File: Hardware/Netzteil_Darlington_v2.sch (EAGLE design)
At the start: 149 parts, among them IC1 7815TV, IC11 OPA2197, IC12 MAX4080F, IC13 OPA2197, IC15 LD33V, IC17 7815TV, IC18 7812TV, IC2 OPA2197, IC4 LM358ADR, IC5 OPA2197, IC6 TPS5430, IC9 LM334, T1 IRLL110TRPBF, T3 BD139, T4 2N5401, T5 TIP3055, T6 TIP3055, T7 BD139, T8 BC847ALT1G, T9 BUJ303B,127

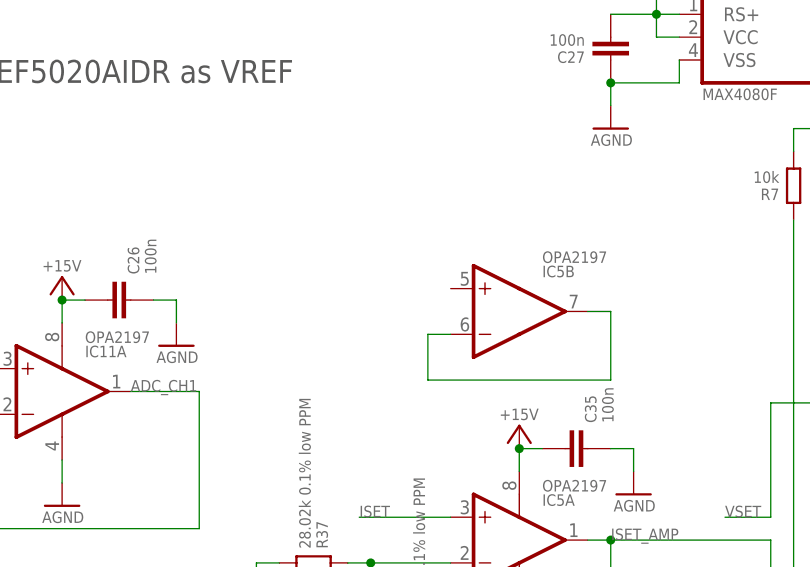
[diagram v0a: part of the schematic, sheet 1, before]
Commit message: Add files via upload
fix second, floating, unused ISET opamp (IC5B)
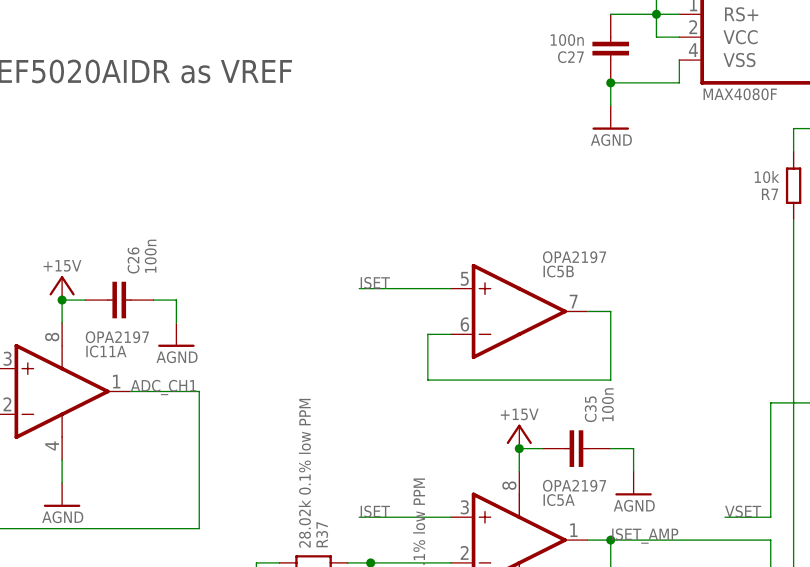
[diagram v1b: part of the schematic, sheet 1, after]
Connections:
- net ISET: now also IC5B.+IN
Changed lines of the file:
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@@
 <setting verticaltext="up"/>
 </settings>
-<grid distance="1.27" unitdist="mm" unit="mm" style="lines" multiple="1" display="yes" altdistance="0.01" altunitdist="inch" altunit="inch"/>
+<grid distance="2.54" unitdist="mm" unit="mm" style="lines" multiple="1" display="yes" altdistance="0.01" altunitdist="inch" altunit="inch"/>
 <layers>
 <layer number="1" name="Top" color="4" fill="1" visible="no" active="no"/>
@@
 <label x="86.36" y="96.52" size="1.27" layer="95"/>
 </segment>
-</net>
+<segment>
+<pinref part="IC5" gate="B" pin="+IN"/>
+<wire x1="96.52" y1="121.92" x2="86.36" y2="121.92" width="0.1524" layer="91"/>
+<label x="86.36" y="121.92" size="1.27" layer="95"/>
+</segment>
+</net>

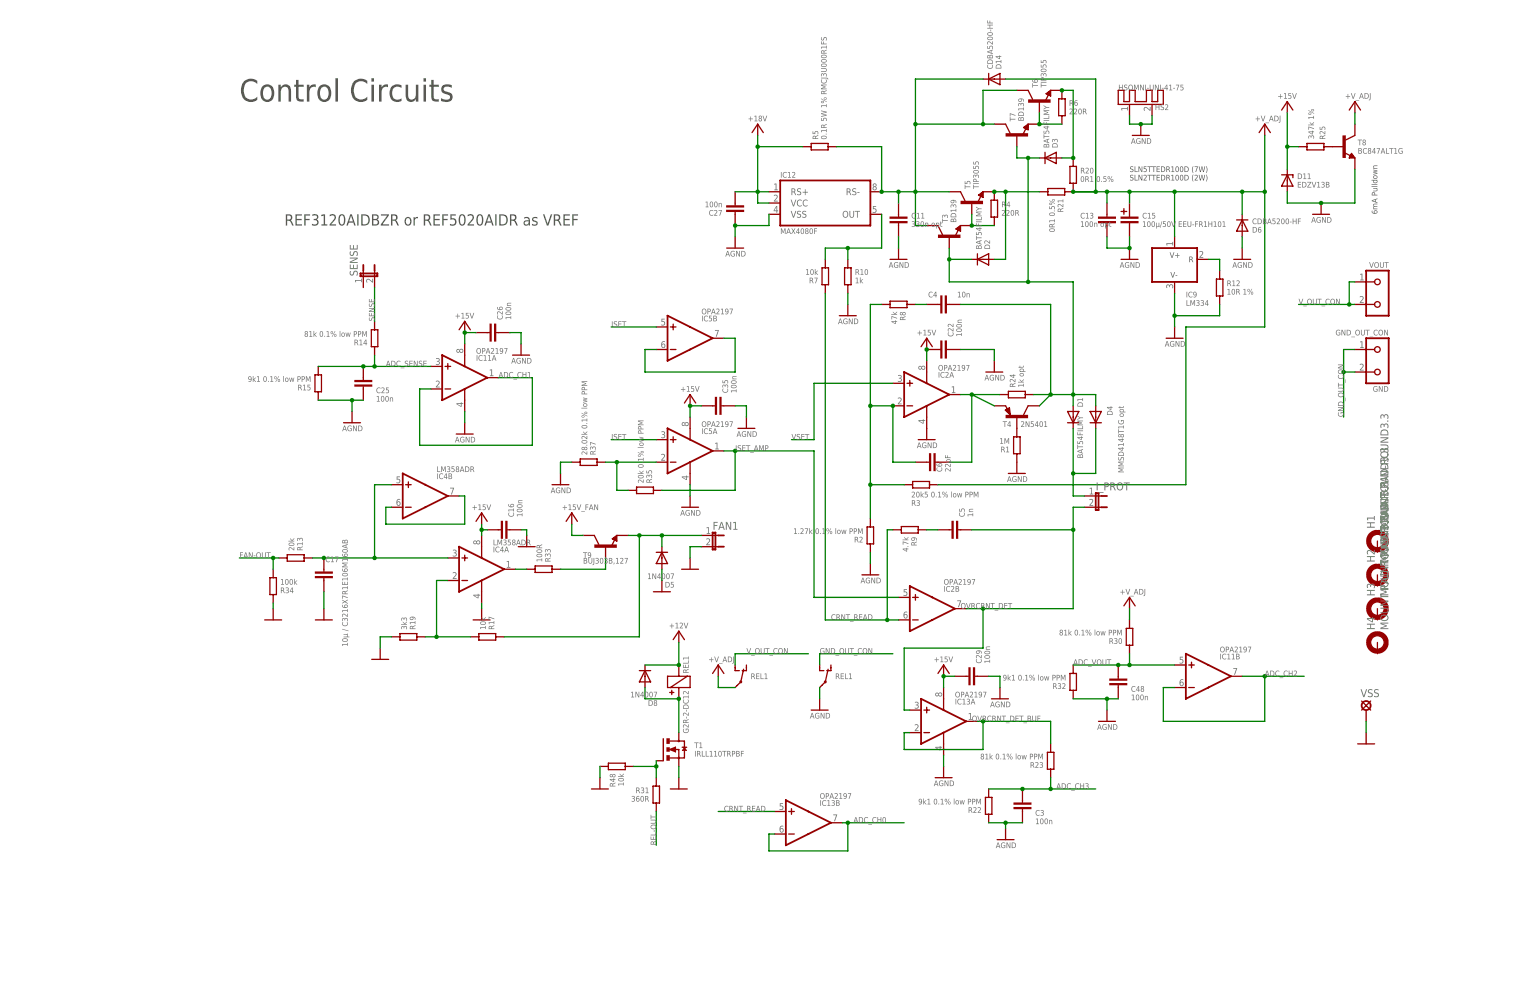
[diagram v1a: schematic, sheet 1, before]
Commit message: update to rev 1.6
fix several bugs and issues
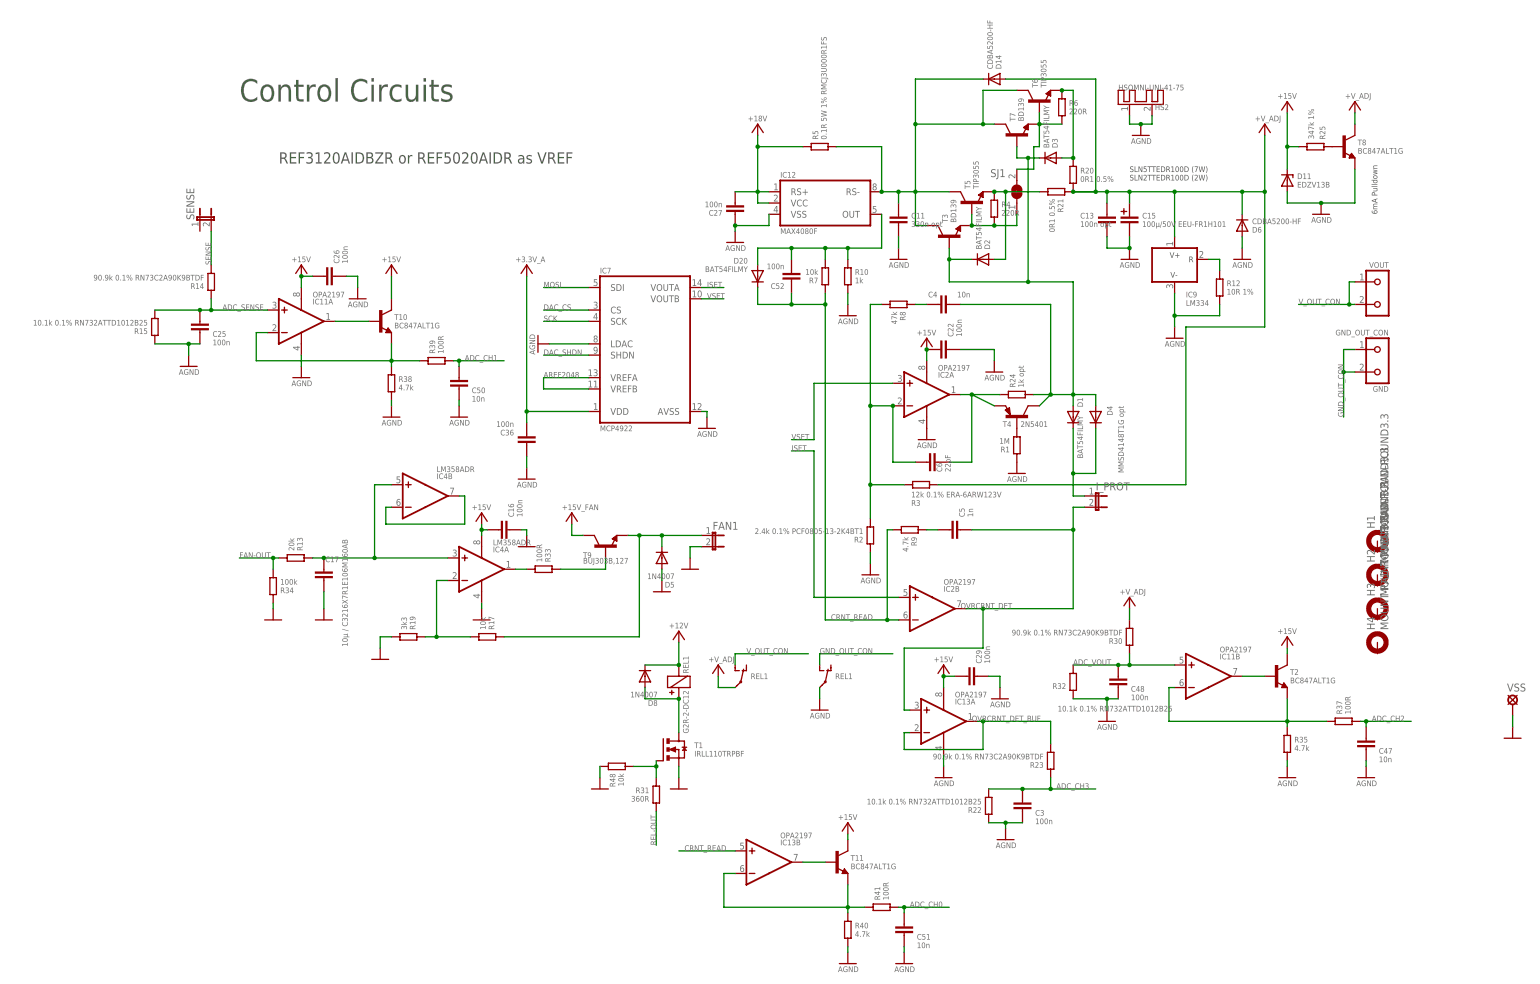
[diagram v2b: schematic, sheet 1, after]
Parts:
- removed ETHERNET: (no value), con-lsta:FE08-1
- added C36, C46, C52: 100n, goujine:CC/0805
- added C44, C45: 10µ / C3216X7R1E106M160AB, goujine:CC/1206
- added C47, C50, C51: 10n, goujine:CC/0805
- added D13: 1N4007, diode:DIODE-DO214AA
- added D20: BAT54FILMY, neumluc:DBAT54FILMY
- added ESP: (no value), con-lstb:MA06-1
- added IC7: MCP4922, neumluc:MCP4922
- added L5: MPZ2012S601AT000, neumluc:L0805
- added R38, R40: 4.7k, neumluc:R-SMD0805
- added R39, R41: 100R, neumluc:R-SMD0805
- added SJ1: (no value), jumper:SJ
- added T10, T11, T2: BC847ALT1G, neumluc:T-NPNSOT23-BEC
- IC5: value OPA2197 -> LD33V; device goujine:DUAL-OPVSOP8 -> neumluc:LD33V
- R14, R23, R30: value 81k 0.1% low PPM -> 90.9k 0.1% RN73C2A90K9BTDF
- R15, R22, R32: value 9k1 0.1% low PPM -> 10.1k 0.1% RN732ATTD1012B25
- R18: value 2k5 -> 2k2
- R2: value 1.27k 0.1% low PPM -> 2.4k 0.1% PCF0805-13-2K4BT1
- R3: value 20k5 0.1% low PPM -> 12k 0.1% ERA-6ARW123V
- R35: value 20k 0.1% low PPM -> 4.7k
- R37: value 28.02k 0.1% low PPM -> 100R
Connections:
- removed net +3.3V_LP: C7.1, C8.1, IC3.IN, U$33.3V3_LO
- removed net ETH_CS: ETHERNET.6, U$33.28
- removed net ETH_INT: ETHERNET.4, U$33.25
- removed net ETH_RST: ETHERNET.1, U$33.7
- removed net ISET_AMP: IC2B.+IN, IC5A.OUT, R35.1
- removed net RESET: U$33.RESET
- new net +3.3V_A: C36.2, C45.1, C46.1, C7.1, C8.1, IC3.IN, IC7.VDD, L5.2
- new net DAC_CS: IC7.CS, U$33.14/A0
- new net DAC_SHDN: IC7.SHDN, U$33.A22/DAC1
- new net ESP-IO: ESP.5, U$33.10/CS
- new net ESP-RST: ESP.3, U$33.28
- new net ESP-RX: ESP.2, U$33.31/A12
- new net ESP-TX: ESP.1, U$33.32/A13
- new net N$41: IC11B.-IN, R35.1, R37.1, T2.E
- new net N$42: IC11A.OUT, T10.B
- new net N$43: IC11A.-IN, R38.1, R39.1, T10.E
- new net N$44: IC13B.OUT, T11.B
- new net N$45: IC13B.-IN, R40.1, R41.1, T11.E
- net +15V: now also D13.C, IC5.VI, T10.C, T11.C, T2.C; no longer IC5PWR.V+
- net +3.3V: now also ESP.4; no longer ETHERNET.7
- net ADC_CH0: now also C51.1, R41.2, U$33.20/A6; no longer IC13B.-IN, IC13B.OUT, U$33.15/A1
- net ADC_CH1: now also C50.1, R39.2; no longer IC11A.-IN, IC11A.OUT
- net ADC_CH2: now also C47.1, R37.2; no longer IC11B.-IN, IC11B.OUT
- net ADC_CH3: now also U$33.19/A5/SCL; no longer U$33.14/A0
- net AGND: now also C36.1, C44.1, C45.2, C46.2, C47.2, C50.2, C51.2, IC5.GND, IC7.AVSS, IC7.LDAC, R35.2, R38.2, R40.2; no longer IC5PWR.V-, R37.2
- net AREF2048: now also IC7.VREFA, IC7.VREFB
- net CRNT_READ: now also C52.1, D20.C
- net ENC_A: now also U$33.21/A7; no longer U$33.20/A6
- net ENC_B: now also U$33.22/A8; no longer U$33.21/A7
- net ENC_BTN: now also U$33.23/A9; no longer U$33.22/A8
- net FAN-OUT: now also U$33.29; no longer U$33.30
- net ISET: now also IC2B.+IN, IC7.VOUTA; no longer IC5A.+IN, IC5B.+IN, U$33.A22/DAC1
- net MISO: no longer ETHERNET.2
- net MOSI: now also IC7.SDI; no longer ETHERNET.3
- net N$15: now also SJ1.1
- net N$39: now also C44.2, D13.A, IC5.VO, L5.1; no longer IC5B.-IN, IC5B.OUT
- net N$40: now also IC11B.OUT, T2.B; no longer IC5A.-IN, R35.2, R37.1
- net N$5: now also SJ1.2
- net N$7: now also C52.2, D20.A
- net REL-OUT: now also U$33.30; no longer U$33.32/A13
- net SCK: now also IC7.SCK; no longer ETHERNET.5
- net VSET: now also IC7.VOUTB; no longer U$33.A21/DAC0
- net VSS: now also ESP.6; no longer ETHERNET.8
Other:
- moved on the sheet: C25, C26, IC11A, IC13B, R14, R15, R35, R37, SENSE, VSS
